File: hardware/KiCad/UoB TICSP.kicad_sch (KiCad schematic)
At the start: 26 parts, among them J1 Wago 233-503, J2 SMA, J3 PT02A12-4PW, J4 Wago 233-506, SW1 R13-527B-02-BB, U1 LT3045EDD, U2 LT3094EDD

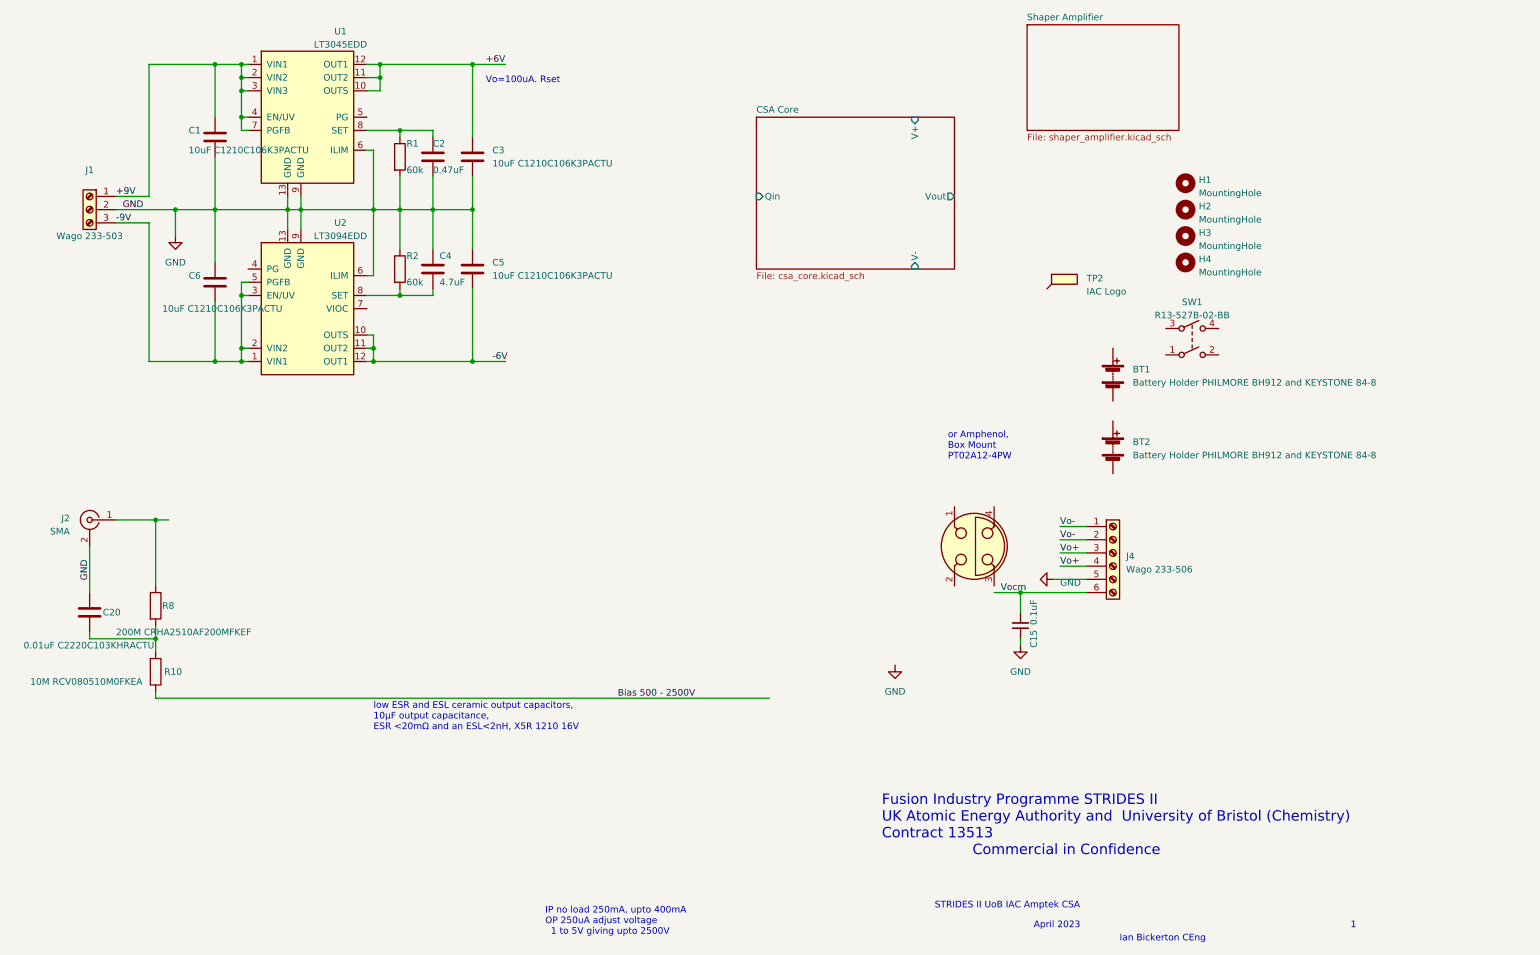
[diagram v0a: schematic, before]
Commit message: More schemataic tidying. Added a csa_core_simulation.kicad_pro to simulate CSA core. Tidied csa_core to make it simulatable, but needs work - OP analysis doesn't converge at the moment. (Need to fiddle with op-amp compensation??)
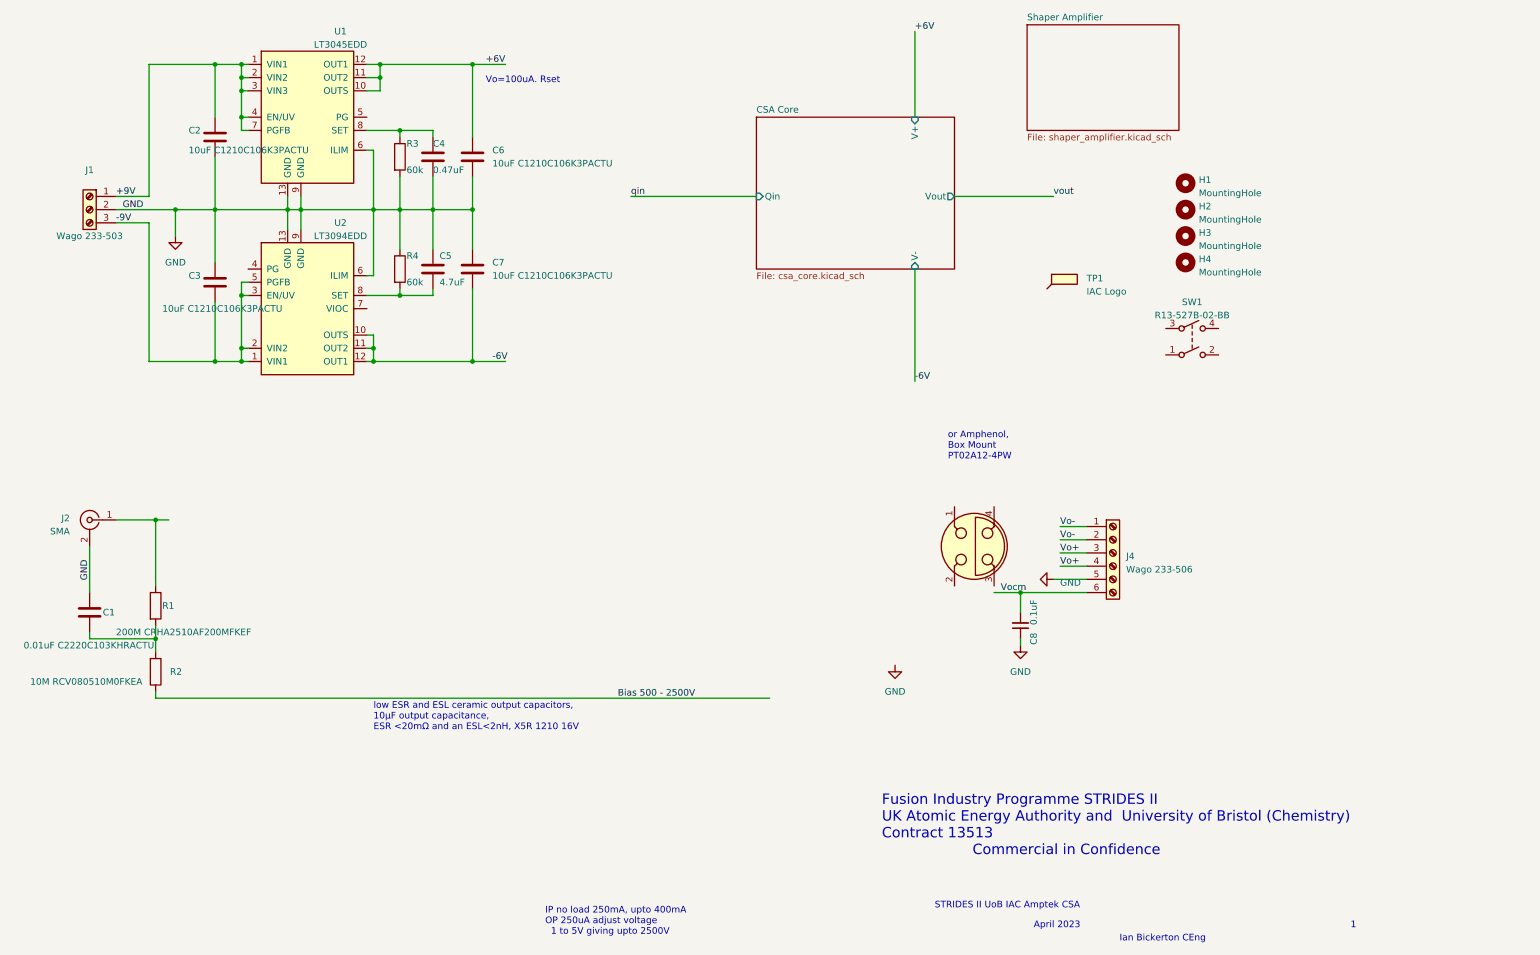
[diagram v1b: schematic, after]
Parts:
- removed BT1, BT2: Battery Holder PHILMORE BH912 and KEYSTONE 84-8, symbol Device:Battery
- SW1: footprint (none) -> Button_Switch_SMD:SW_DIP_SPSTx02_Slide_6.7x6.64mm_W6.73mm_P2.54mm_LowProfile_JPin
- renumbered C20 to C1, C1 to C2, C6 to C3, C2 to C4, C4 to C5, C3 to C6, C5 to C7, C15 to C8, R8 to R1, R10 to R2, R1 to R3, R2 to R4, TP2 to TP1

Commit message: End of day save. Just needs voids added to planes to reduce capacitance
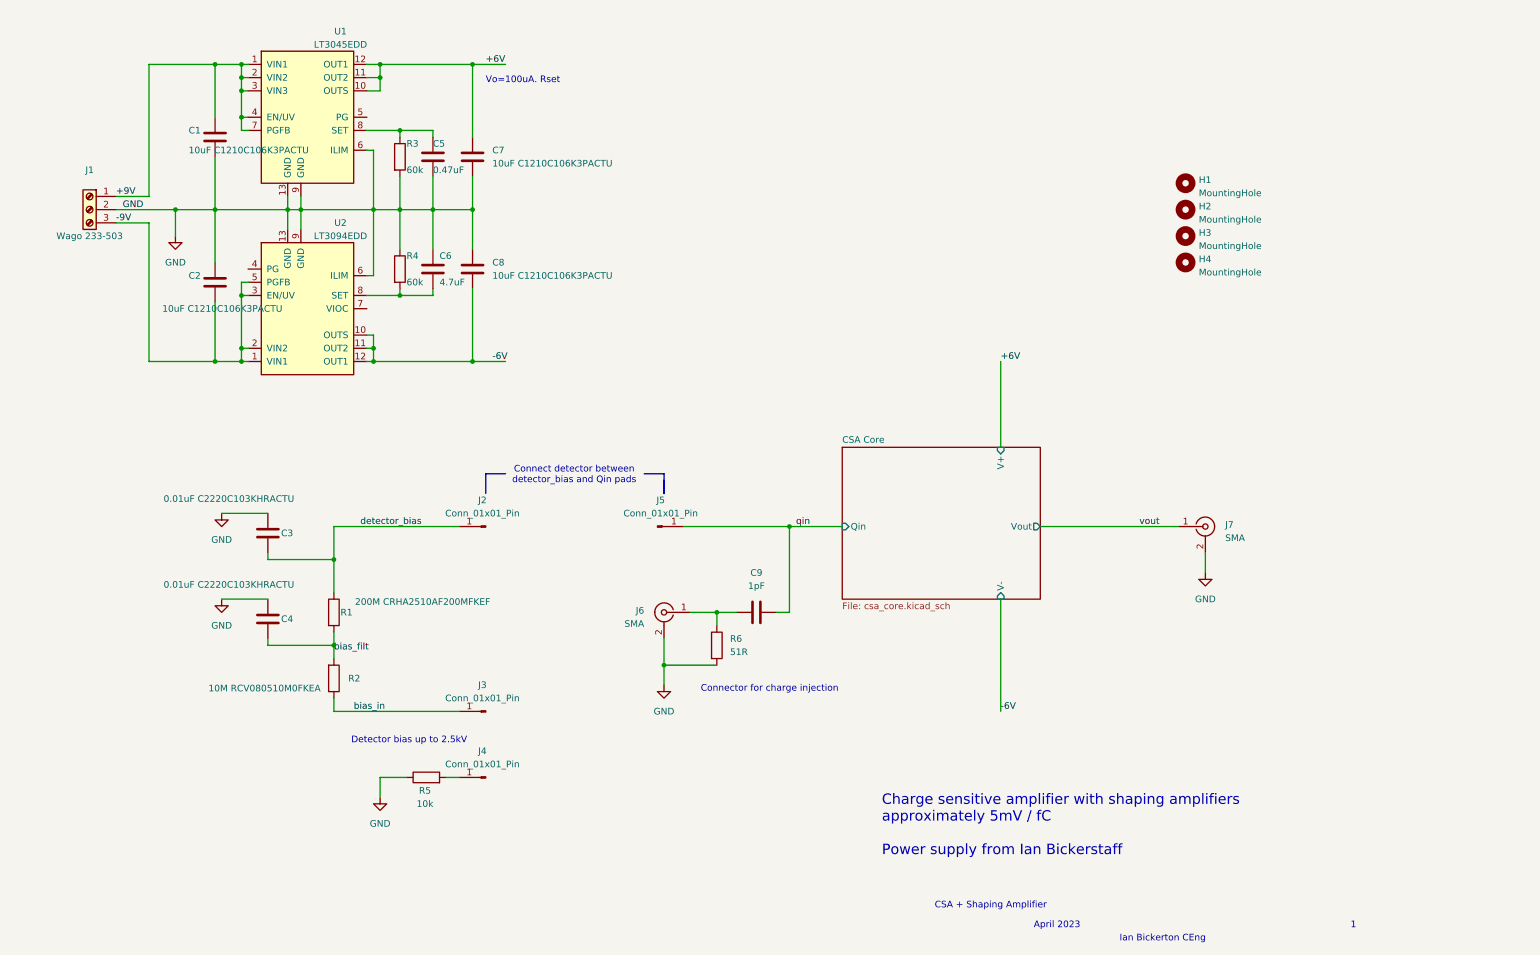
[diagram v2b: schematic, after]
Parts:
- removed C8: 0.1uF, Capacitor_SMD:C_0805_2012Metric, symbol Device:C_Small
- removed J3: PT02A12-4PW, TestPoint:TestPoint_Pad_D1.0mm, symbol Connector:LEMO4
- removed J4: Wago 233-506, UoB Cremat Library:TerminalBlock_WAGO_233-506_1x06_P2.54mm_45Degree, symbol Connector:Screw_Terminal_01x06
- removed SW1: R13-527B-02-BB, Button_Switch_SMD:SW_DIP_SPSTx02_Slide_6.7x6.64mm_W6.73mm_P2.54mm_LowProfile_JPin, symbol Switch:SW_DPST
- removed TP1: IAC Logo, UoB Cremat Library:IAC Logo, symbol Connector:TestPoint_Flag
- added C3: 0.01uF C2220C103KHRACTU, Capacitor_SMD:C_2220_5750Metric_Pad1.97x5.40mm_HandSolder, symbol Device:C
- added C9: 1pF, Capacitor_SMD:C_0603_1608Metric_Pad1.08x0.95mm_HandSolder, symbol Device:C
- added J2, J3, J4, J5: Conn_01x01_Pin, Connector_Wire:SolderWire-2sqmm_1x01_D2mm_OD3.9mm, symbol Connector:Conn_01x01_Pin
- added J7: SMA, Connector_Coaxial:SMA_Amphenol_901-144_Vertical, symbol Connector:Conn_Coaxial
- added R5: 10k, Resistor_SMD:R_0805_2012Metric_Pad1.20x1.40mm_HandSolder, symbol Device:R
- added R6: 51R, Resistor_SMD:R_0603_1608Metric_Pad0.98x0.95mm_HandSolder, symbol Device:R
- C4: renamed from C1; footprint Capacitor_SMD:C_2220_5650Metric -> Capacitor_SMD:C_2220_5750Metric_Pad1.97x5.40mm_HandSolder
- H1, H2, H3, H4: footprint MountingHole:MountingHole_2.2mm_M2_DIN965 -> MountingHole:MountingHole_2.7mm_M2.5
- J6: renamed from J2; footprint Connector_Coaxial:SMA_Amphenol_901-143_Horizontal -> Connector_Coaxial:SMA_Amphenol_901-144_Vertical
- renumbered C2 to C1, C3 to C2, C4 to C5, C5 to C6, C6 to C7, C7 to C8
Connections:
- net GND: now also C3.2, J7.2 (Ext), R5.1, R6.2
- net qin: now also C9.2, J5.1 (Pin_1)
- net vout: now also J7.1 (In)
- net at J6.1 (In): now also C9.1, R6.1; no longer R1.1
- net bias_filt: now reaches C4.1, R1.2, R2.2
- net Bias 500 - 2500V renamed bias_in
- net bias_in: now also J3.1 (Pin_1)
- new net: J4.1 (Pin_1), R5.2
- new net detector_bias: C3.1, J2.1 (Pin_1), R1.1
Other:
- removed sheet Shaper Amplifier
- note added: "CSA + Shaping Amplifier"
- note added: "Charge sensitive amplifier with shaping amplifiers approximately 5mV / fC Power supply from Ian Bickerstaff"
- note added: "Connect detector between detector_bias and Qin pads"
- note added: "Connector for charge injection"
- note added: "Detector bias up to 2.5kV"
- note removed: "Fusion Industry Programme STRIDES II UK Atomic Energy Authority and University of Bristol (Chemistry) Contract 13513 Commercial in Confidence"
- note removed: "IP no load 250mA, upto 400mA OP 250uA adjust voltage 1 to 5V giving upto 2500V"
- note removed: "STRIDES II UoB IAC Amptek CSA"
- note removed: "low ESR and ESL ceramic output capacitors, 10µF output capacitance, ESR <20mΩ and an ESL<2nH, X5R 1210 16V"
- note removed: "or Amphenol, Box Mount PT02A12-4PW"
- moved on the sheet: C4, J6, R1, R2

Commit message: Generated artwork
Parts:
- removed U1: LT3045EDD, Package_SO:MSOP-12-1EP_3x4mm_P0.65mm_EP1.65x2.85mm, symbol UoB Diamond Sensor Library:LT3045
- removed U2: LT3094EDD, Package_SO:MSOP-12-1EP_3x4mm_P0.65mm_EP1.65x2.85mm, symbol UoB Diamond Sensor Library:LT3094
- added R17, R18: 240, Resistor_SMD:R_0603_1608Metric_Pad0.98x0.95mm_HandSolder, symbol Device:R
- added U6: LM317_SOT-223, Package_TO_SOT_SMD:SOT-223-3_TabPin2, symbol Regulator_Linear:LM317_SOT-223
- added U7: LM337_SOT223, Package_TO_SOT_SMD:SOT-223-3_TabPin2, symbol Regulator_Linear:LM337_SOT223
- C5: value 0.47uF -> 10uF C1210C106K3PACTU; footprint Capacitor_SMD:C_1206_3216Metric -> Capacitor_SMD:C_1210_3225Metric
- C6: value 4.7uF -> 10uF C1210C106K3PACTU; footprint Capacitor_SMD:C_1206_3216Metric -> Capacitor_SMD:C_1210_3225Metric
- R3: value 60k -> 1.8k; footprint Resistor_SMD:R_0805_2012Metric -> Resistor_SMD:R_0603_1608Metric_Pad0.98x0.95mm_HandSolder
- R4: value 60k -> 1k; footprint Resistor_SMD:R_0805_2012Metric -> Resistor_SMD:R_0603_1608Metric_Pad0.98x0.95mm_HandSolder
- R5: value 10k -> 1k; footprint Resistor_SMD:R_0805_2012Metric_Pad1.20x1.40mm_HandSolder -> Resistor_SMD:R_0603_1608Metric_Pad0.98x0.95mm_HandSolder
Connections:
- net -9V: now also U7.2 (VI)
- net GND: now also C5.1, C6.2; no longer C5.2, C6.1
- net at R4.2: now also C5.2, R18.1, U7.1 (ADJ); no longer C6.2
- net at R3.1: now also C6.1, R17.2, U6.1 (ADJ); no longer C5.1
- net +6V renamed +10V
- net +10V: now also R17.1, U6.2 (VO)
- net +9V renamed +12V
- net +12V: now also U6.3 (VI)
- net -6V renamed V-
- net V-: now also R18.2, U7.3 (VO)
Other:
- note removed: "Vo=100uA. Rset"
- moved on the sheet: C7, C8, R3, R4

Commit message: Printed PDF schemaics. Saved schematic and PCB as KiCAD 9
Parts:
- C9: value 1pF -> 1pF
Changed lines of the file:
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@@
 (kicad_sch
-	(version 20231120)
+	(version 20250114)
 	(generator "eeschema")
-	(generator_version "8.0")
+	(generator_version "9.0")
 	(paper "A4")
+	(text "CSA + Shaping Amplifier\n"
+		(exclude_from_sim no)
+		(at 190.5 190.5 0)
+		(effects
+			(font
+				(size 1.27 1.27)
+			)
+			(justify left bottom)
+		)
+	)
+	(text "Ian Bickerton CEng"
+		(exclude_from_sim no)
+		(at 226.06 196.85 0)
+		(effects
+			(font
+				(size 1.27 1.27)
+			)
+			(justify left bottom)
+		)
+	)
+	(text "Connector for charge injection"
+		(exclude_from_sim no)
+		(at 158.75 148.082 0)
+		(effects
+			(font
+				(size 1.27 1.27)
+			)
+		)
+	)
+	(text "Detector bias up to 2.5kV"
+		(exclude_from_sim no)
+		(at 89.408 157.988 0)
+		(effects
+			(font
+				(size 1.27 1.27)
+			)
+		)
+	)
+	(text "Charge sensitive amplifier with shaping amplifiers\napproximately 5mV / fC\n\nPower supply from Ian Bickerstaff \n"
+		(exclude_from_sim no)
+		(at 180.34 180.34 0)
+		(effects
+			(font
+				(size 2 2)
+			)
+			(justify left bottom)
+		)
+	)
+	(text "1"
+		(exclude_from_sim no)
+		(at 270.51 194.31 0)
+		(effects
+			(font
+				(size 1.27 1.27)
+			)
+			(justify left bottom)
+		)
+	)
+	(text "Connect detector between\ndetector_bias and Qin pads"
+		(exclude_from_sim no)
+		(at 121.158 106.934 0)
+		(effects
+			(font
+				(size 1.27 1.27)
+			)
+		)
+	)
+	(text "April 2023"
+		(exclude_from_sim no)
+		(at 209.55 194.31 0)
+		(effects
+			(font
+				(size 1.27 1.27)
+			)
+			(justify left bottom)
+		)
+	)
 	(junction
 		(at 74.93 139.7)
@@
 		)
 	)
-	(text "CSA + Shaping Amplifier\n"
-		(exclude_from_sim no)
-		(at 190.5 190.5 0)
-		(effects
-			(font
-				(size 1.27 1.27)
-			)
-			(justify left bottom)
-		)
-	)
-	(text "Ian Bickerton CEng"
-		(exclude_from_sim no)
-		(at 226.06 196.85 0)
-		(effects
-			(font
-				(size 1.27 1.27)
-			)
-			(justify left bottom)
-		)
-	)
-	(text "Connector for charge injection"
-		(exclude_from_sim no)
-		(at 158.75 148.082 0)
-		(effects
-			(font
-				(size 1.27 1.27)
-			)
-		)
-	)
-	(text "Detector bias up to 2.5kV"
-		(exclude_from_sim no)
-		(at 89.408 157.988 0)
-		(effects
-			(font
-				(size 1.27 1.27)
-			)
-		)
-	)
-	(text "Charge sensitive amplifier with shaping amplifiers\napproximately 5mV / fC\n\nPower supply from Ian Bickerstaff \n"
-		(exclude_from_sim no)
-		(at 180.34 180.34 0)
-		(effects
-			(font
-				(size 2 2)
-			)
-			(justify left bottom)
-		)
-	)
-	(text "1"
-		(exclude_from_sim no)
-		(at 270.51 194.31 0)
-		(effects
-			(font
-				(size 1.27 1.27)
-			)
-			(justify left bottom)
-		)
-	)
-	(text "Connect detector between\ndetector_bias and Qin pads"
-		(exclude_from_sim no)
-		(at 121.158 106.934 0)
-		(effects
-			(font
-				(size 1.27 1.27)
-			)
-		)
-	)
-	(text "April 2023"
-		(exclude_from_sim no)
-		(at 209.55 194.31 0)
-		(effects
-			(font
-				(size 1.27 1.27)
-			)
-			(justify left bottom)
-		)
-	)
 	(label "+12V"
 		(at 33.02 53.34 0)
-		(fields_autoplaced yes)
 		(effects
 			(font
@@
 	(label "+10V"
 		(at 115.57 27.94 0)
-		(fields_autoplaced yes)
 		(effects
 			(font
@@
 	(label "-9V"
 		(at 33.02 58.42 0)
-		(fields_autoplaced yes)
 		(effects
 			(font
@@
 	(label "V-"
 		(at 116.84 85.09 0)
-		(fields_autoplaced yes)
 		(effects
 			(font
@@
 	(label "bias_in"
 		(at 78.74 152.4 0)
-		(fields_autoplaced yes)
 		(effects
 			(font
@@
 	(label "bias_filt"
 		(at 74.93 140.97 0)
-		(fields_autoplaced yes)
 		(effects
 			(font
@@
 	(label "detector_bias"
 		(at 80.01 116.84 0)
-		(fields_autoplaced yes)
 		(effects
 			(font
@@
 	(label "V-"
 		(at 203.2 152.4 0)
-		(fields_autoplaced yes)
 		(effects
 			(font
@@
 	(label "vout"
 		(at 229.87 116.84 0)
-		(fields_autoplaced yes)
 		(effects
 			(font
@@
 	(label "+10V"
 		(at 203.2 85.09 0)
-		(fields_autoplaced yes)
 		(effects
 			(font
@@
 	(label "GND"
 		(at 34.29 55.88 0)
-		(fields_autoplaced yes)
 		(effects
 			(font
@@
 	(label "qin"
 		(at 163.83 116.84 0)
-		(fields_autoplaced yes)
 		(effects
 			(font
@@
 			)
 		)
-		(property "Value" "1pF	"
+		(property "Value" "1pF"
 			(at 156.21 128.27 90)
 			(effects
@@
 		(at 172.72 101.6)
 		(size 38.1 29.21)
+		(exclude_from_sim no)
+		(in_bom yes)
+		(on_board yes)
+		(dnp no)
 		(fields_autoplaced yes)
 		(stroke
@@
 		)
 	)
+	(embedded_fonts no)
 )
